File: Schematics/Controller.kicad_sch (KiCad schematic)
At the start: 0 parts

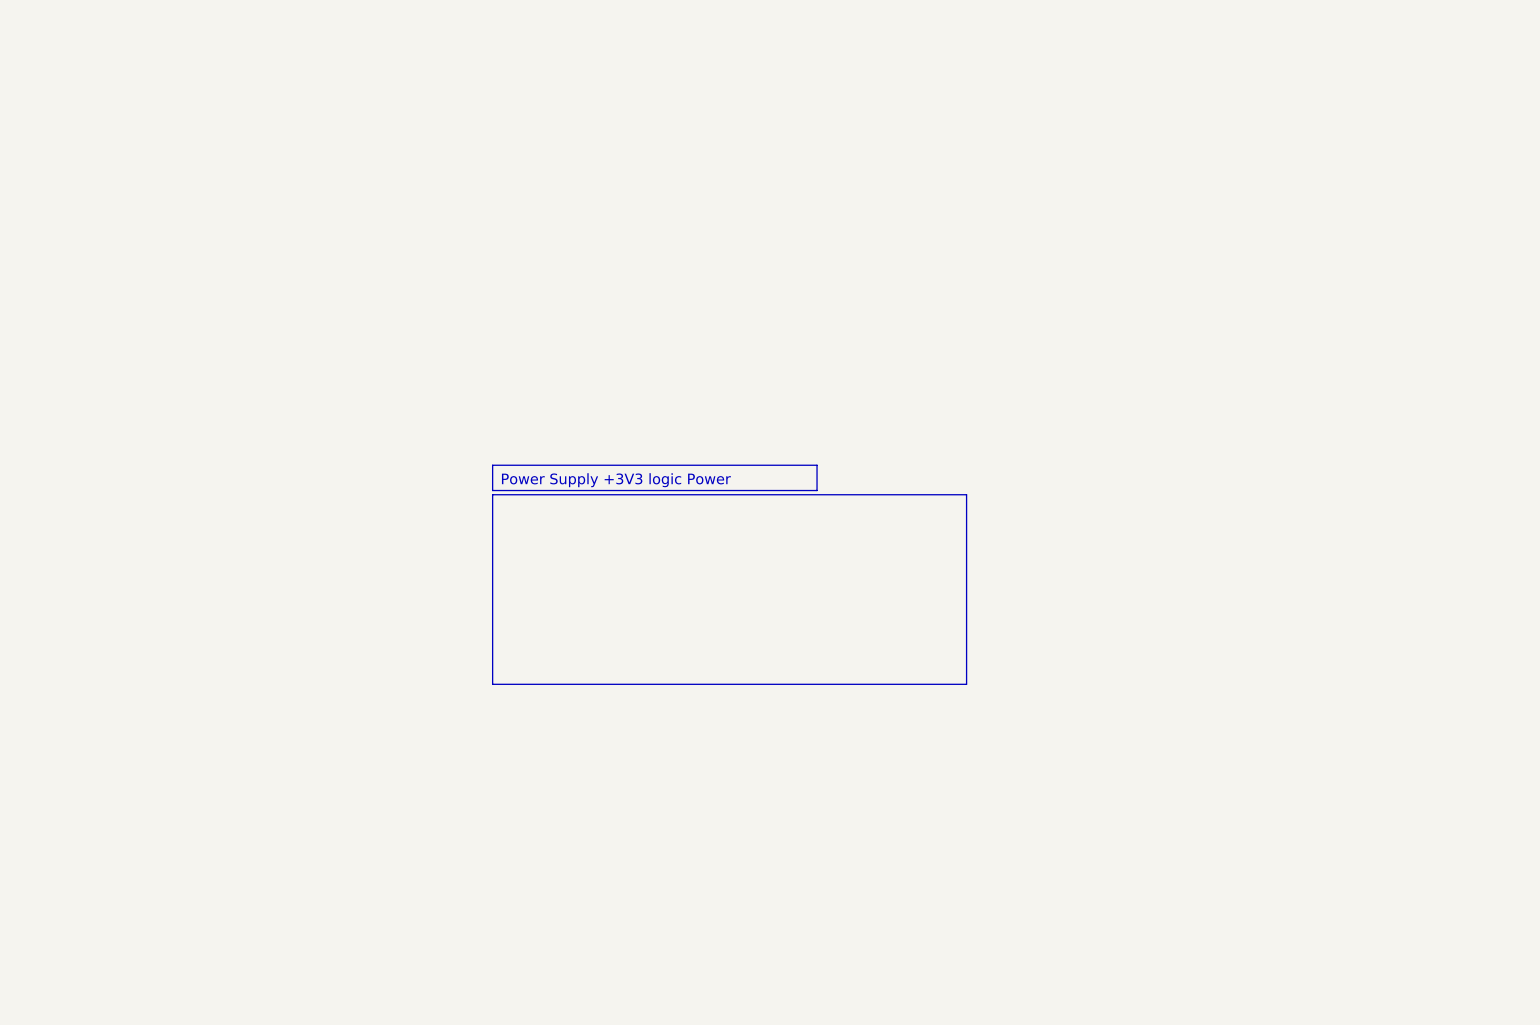
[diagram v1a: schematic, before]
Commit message: [WIP SiC Single Phase Inverter]
- Updated README to have a Block Diagram
- WIP Sub sheets Power, Controller
- Added the F2800 controller to the project
- Added the controller to the controller sub sheet
- Added text for a 15V to 3V3 voltage converter
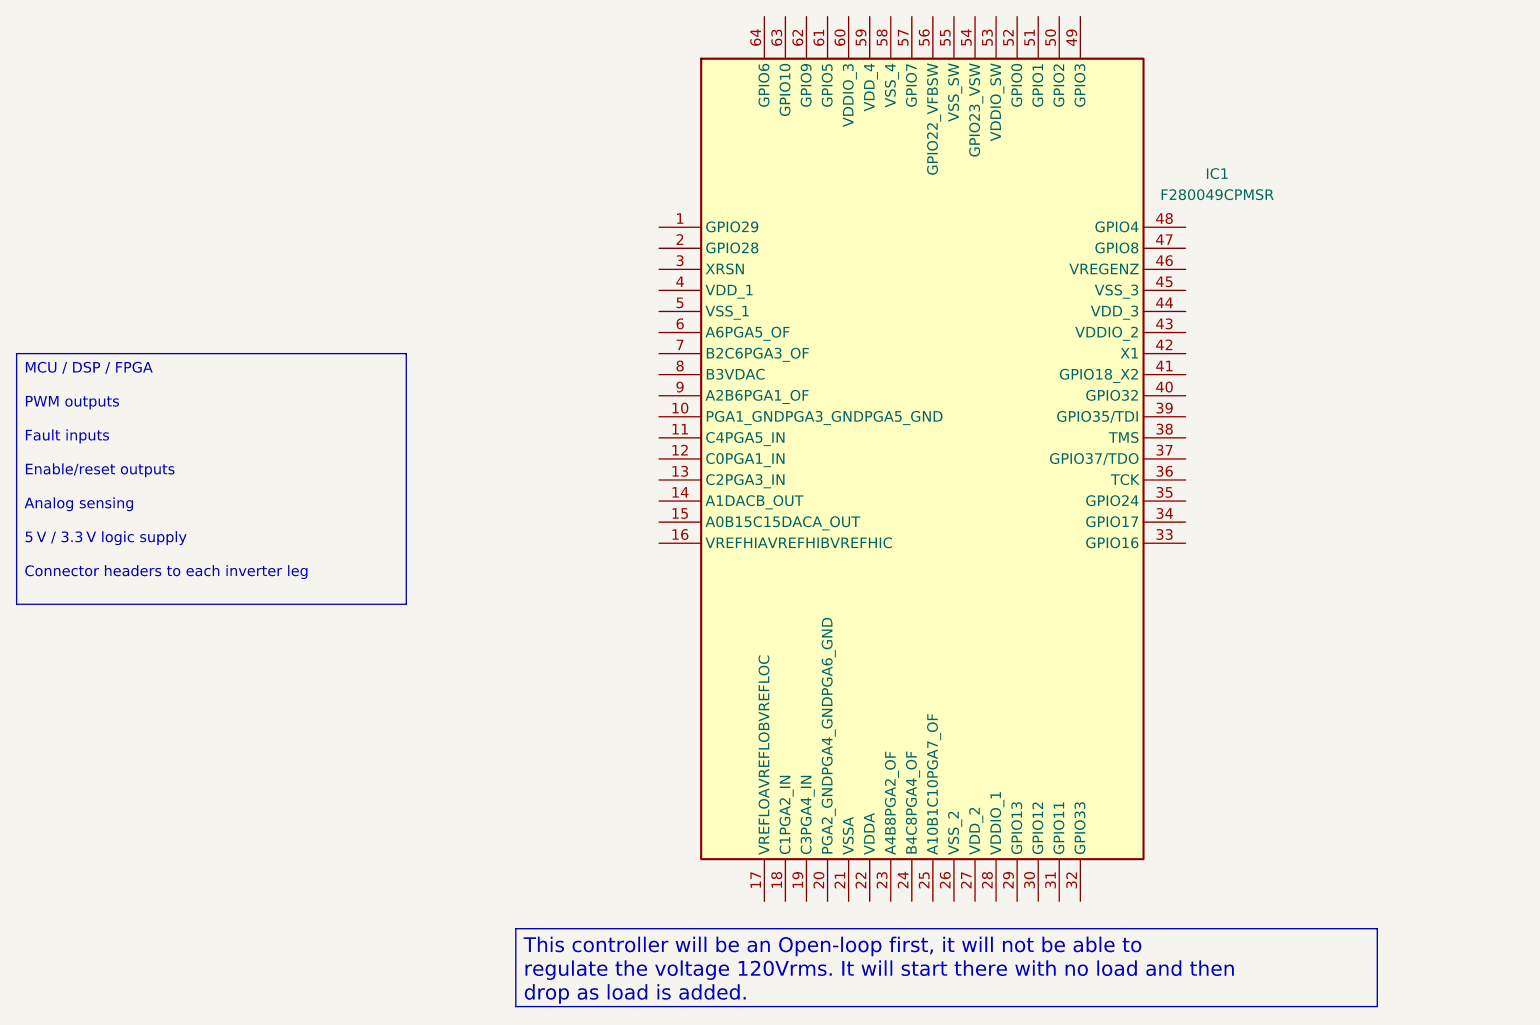
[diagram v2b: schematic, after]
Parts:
- added IC1: F280049CPMSR, SiC_Inverter:F280049CPMSR, symbol SiC_Inverter:F280049CPMSR

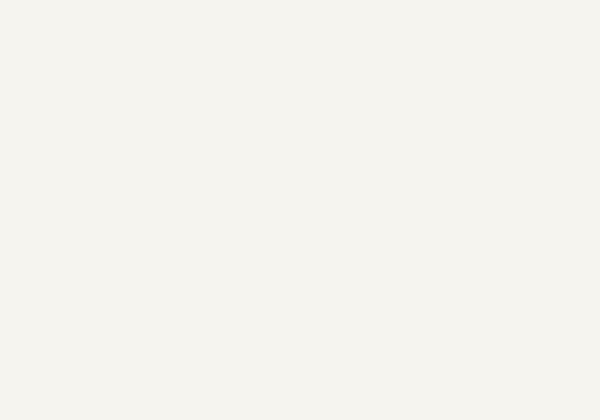
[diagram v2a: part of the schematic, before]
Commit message: [WIP Single Phase Inverter]
- Changed all Refs within each sub sheet (Stripe)
- Added 3V3 Power Supply off of 15V iso supply
- Added footprint, symbol and 3d part
- updated PCB with new part
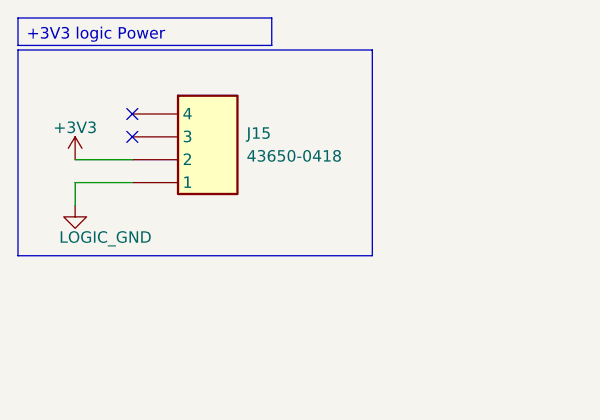
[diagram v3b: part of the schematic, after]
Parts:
- added J15: 43650-0418, SiC_Inverter:436500418, symbol SiC_Inverter:43650-0418
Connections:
- new net +3V3: J15.2
- new net LOGIC_GND: J15.1
- no-connect marks 0 -> 2

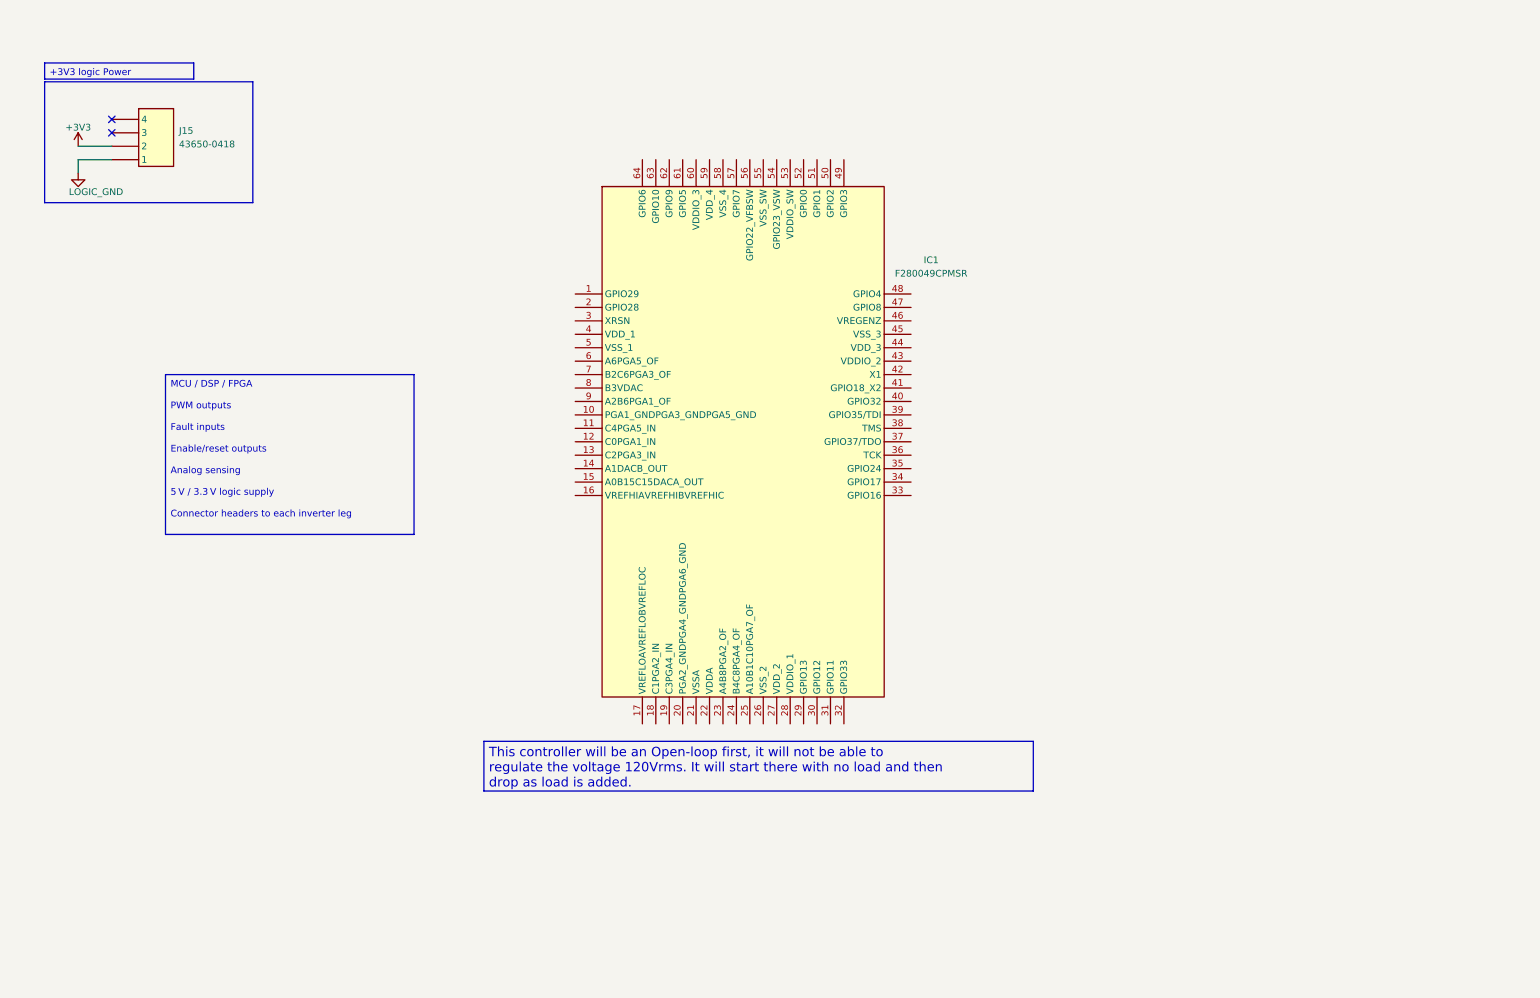
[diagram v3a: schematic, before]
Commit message: WIP: Work on Controller layout, and fixed some sheet text and positions
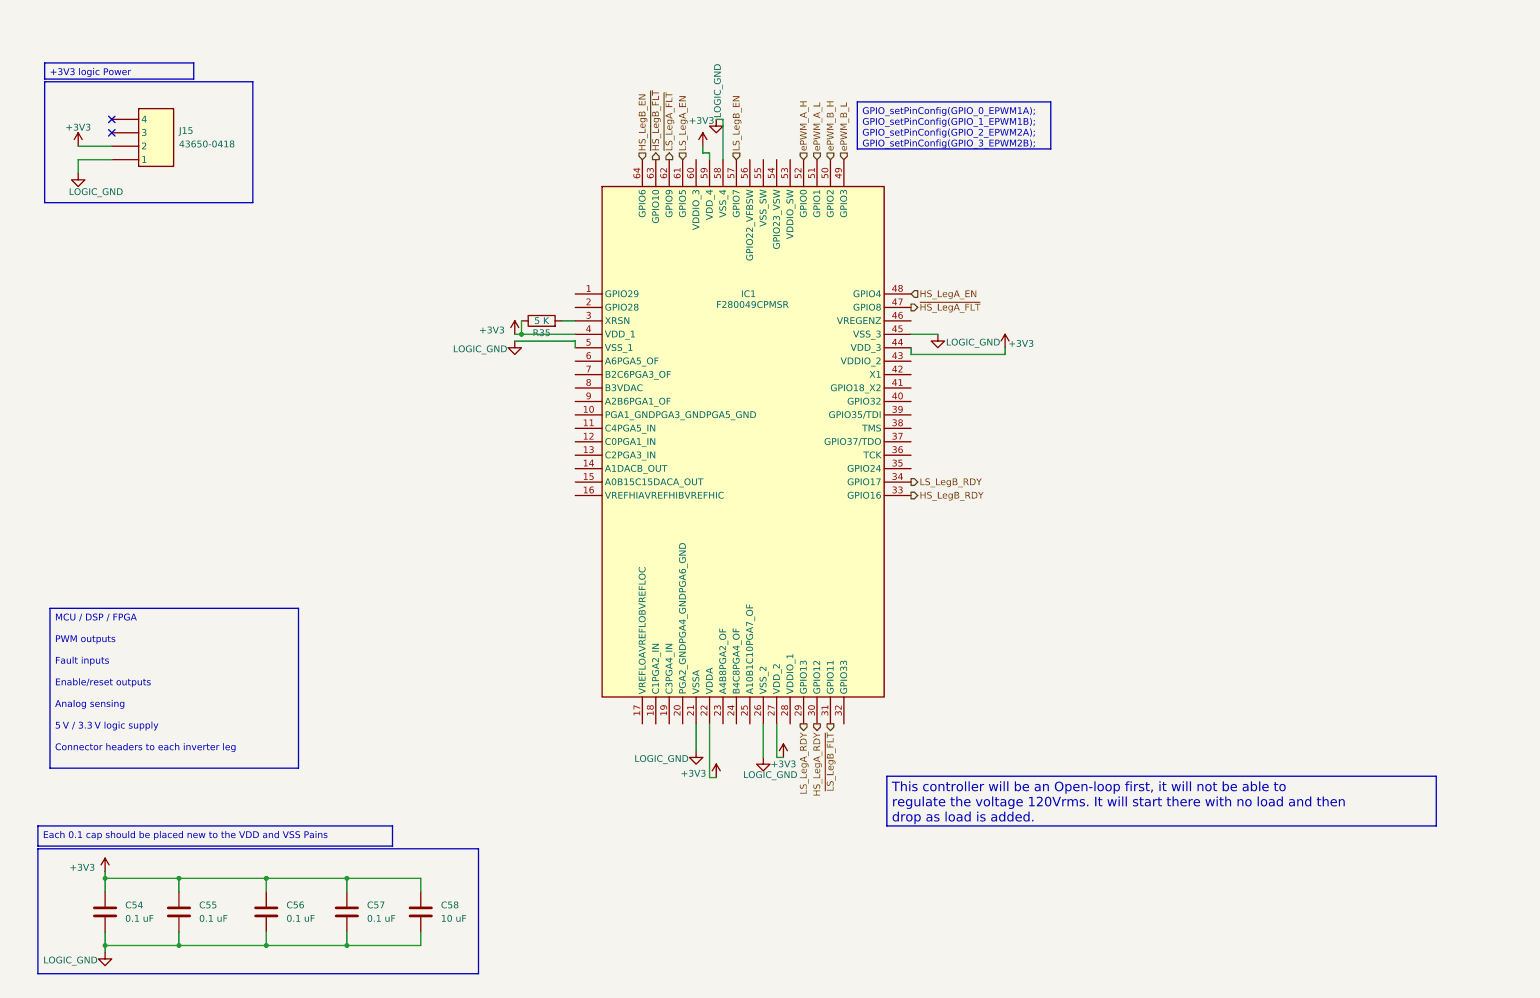
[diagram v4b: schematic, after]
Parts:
- added C54, C55, C56, C57: 0.1 uF, Capacitor_SMD:C_0805_2012Metric_Pad1.18x1.45mm_HandSolder, symbol SiC_Inverter:C2012X8R1E105M125AE
- added C58: 10 uF, Capacitor_SMD:C_0805_2012Metric_Pad1.18x1.45mm_HandSolder, symbol SiC_Inverter:C2012X5R1A106K085AC
- added R35: 5 K, Resistor_SMD:R_1206_3216Metric_Pad1.30x1.75mm_HandSolder, symbol SiC_Inverter:RT1206BRD075KL
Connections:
- net +3V3: now also IC1.22 (VDDA), IC1.27 (VDD_2), IC1.4 (VDD_1), IC1.44 (VDD_3), IC1.59 (VDD_4), C54.1, C55.1, C56.1, C57.1, C58.1, R35.1
- net LOGIC_GND: now also IC1.21 (VSSA), IC1.26 (VSS_2), IC1.45 (VSS_3), IC1.5 (VSS_1), IC1.58 (VSS_4), C54.2, C55.2, C56.2, C57.2, C58.2
- net LS_LegA_RDY: now reaches IC1.29 (GPIO13)
- net at IC1.3 (XRSN): now also R35.2
- net HS_LegA_RDY: now reaches IC1.30 (GPIO12)
- net ~{LS_LegB_FLT}: now reaches IC1.31 (GPIO11)
- net HS_LegB_RDY: now reaches IC1.33 (GPIO16)
- net LS_LegB_RDY: now reaches IC1.34 (GPIO17)
- net ~{HS_LegA_FLT}: now reaches IC1.47 (GPIO8)
- net HS_LegA_EN: now reaches IC1.48 (GPIO4)
- net ePWM_B_L: now reaches IC1.49 (GPIO3)
- net ePWM_B_H: now reaches IC1.50 (GPIO2)
- net ePWM_A_L: now reaches IC1.51 (GPIO1)
- net ePWM_A_H: now reaches IC1.52 (GPIO0)
- net LS_LegB_EN: now reaches IC1.57 (GPIO7)
- net LS_LegA_EN: now reaches IC1.61 (GPIO5)
- net ~{LS_LegA_FLT}: now reaches IC1.62 (GPIO9)
- net ~{HS_LegB_FLT}: now reaches IC1.63 (GPIO10)
- net HS_LegB_EN: now reaches IC1.64 (GPIO6)

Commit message: [WIP Controller Design]
- Wired up all 64 Pins on the Controller
- Added 3d models for connectors and Controller
- Added data sheets for the newly added parts
- wired connectors to controller to external PCB Boards
- Updated Text fields
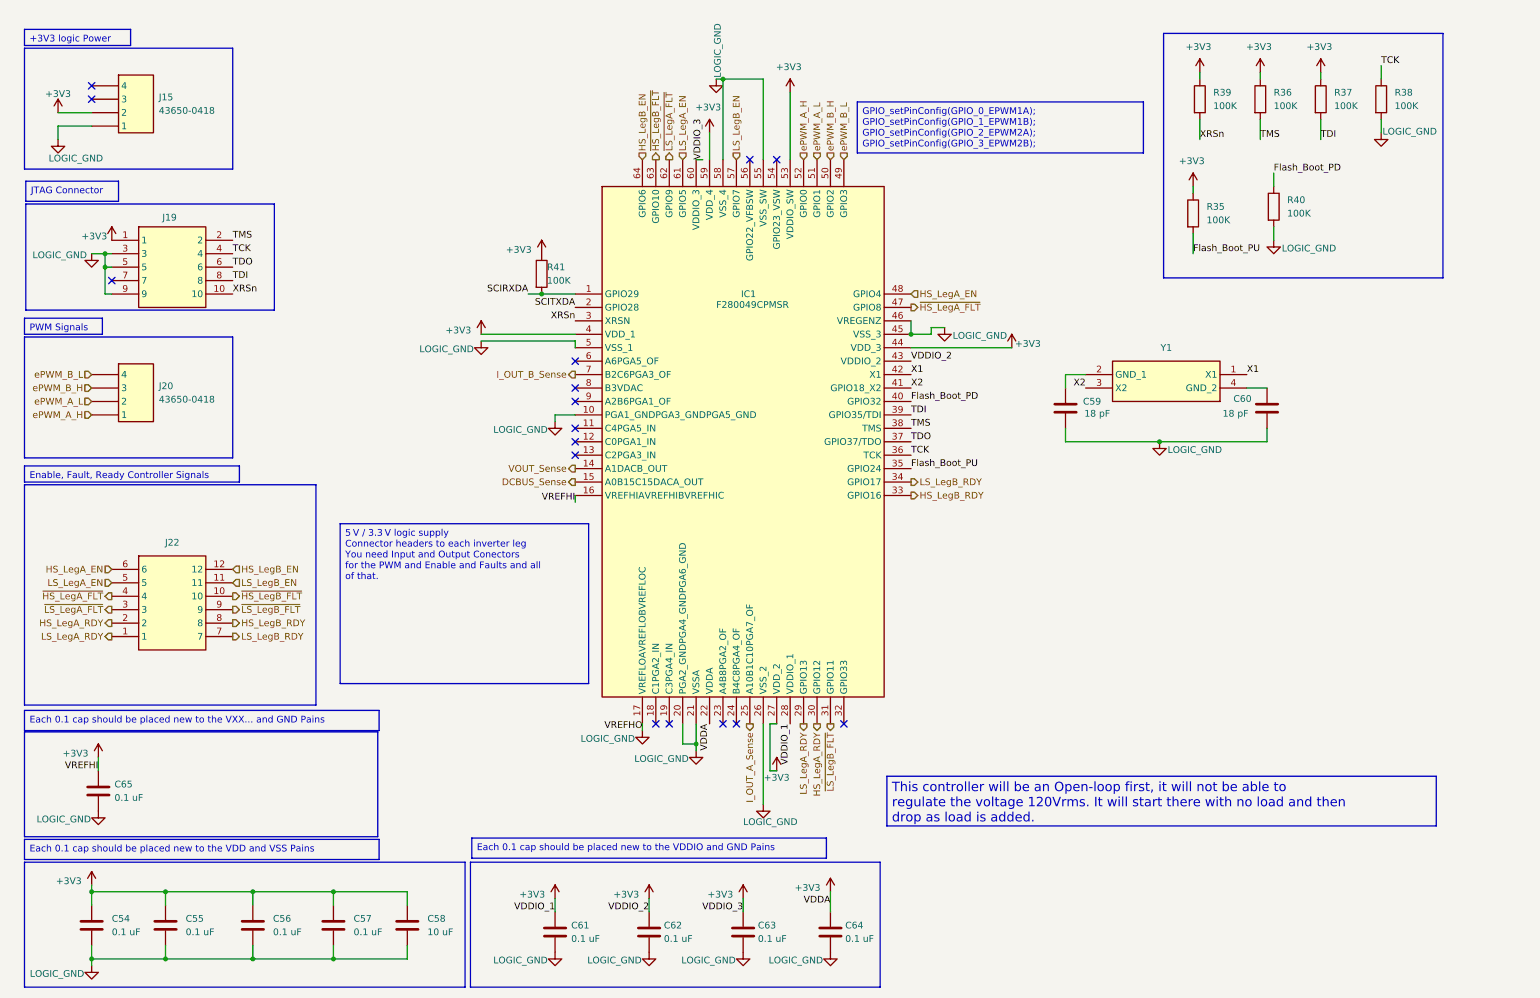
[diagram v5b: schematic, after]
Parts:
- removed R35: 5 K, Resistor_SMD:R_1206_3216Metric_Pad1.30x1.75mm_HandSolder, symbol SiC_Inverter:RT1206BRD075KL
- added C59, C60: 18 pF, Capacitor_SMD:C_0402_1005Metric_Pad0.74x0.62mm_HandSolder, symbol SiC_Inverter:C2012X8R1E105M125AE
- added C61, C62, C63, C64, C65: 0.1 uF, Capacitor_SMD:C_0805_2012Metric_Pad1.18x1.45mm_HandSolder, symbol SiC_Inverter:C2012X8R1E105M125AE
- added J19: FTSH-105-01-LM-D-K, SiC_Inverter:FTSH-105-01-LM-D-K, symbol SiC_Inverter:FTSH-105-01-LM-D-K
- added J20: 43650-0418, SiC_Inverter:436500418, symbol SiC_Inverter:43650-0418
- added J22: 43045-1212, SiC_Inverter:43045-1212, symbol SiC_Inverter:43045-1212
- added R35, R36, R37, R38, R39, R40, R41: 100K, Resistor_SMD:R_1206_3216Metric_Pad1.30x1.75mm_HandSolder, symbol Device:R
- added Y1: ABM8-20.000MHZ-B2-T, SiC_Inverter:ABM8-20.000MHZ-B2-T, symbol SiC_Inverter:ABM8-20.000MHZ-B2-T
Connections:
- net +3V3: now also IC1.16 (VREFHIAVREFHIBVREFHIC), IC1.28 (VDDIO_1), IC1.43 (VDDIO_2), IC1.53 (VDDIO_SW), IC1.60 (VDDIO_3), C61.1, C62.1, C63.1, C64.1, C65.1, J19.1, R35.1, R36.1, R37.1, R39.1, R41.1
- net HS_LegA_EN: now also J22.6
- net HS_LegA_RDY: now also J22.2
- net HS_LegB_EN: now also J22.12
- net HS_LegB_RDY: now also J22.8
- net LOGIC_GND: now also IC1.10 (PGA1_GNDPGA3_GNDPGA5_GND), IC1.17 (VREFLOAVREFLOBVREFLOC), IC1.20 (PGA2_GNDPGA4_GNDPGA6_GND), IC1.46 (VREGENZ), IC1.55 (VSS_SW), C59.2, C60.2, C61.2, C62.2, C63.2, C64.2, C65.2, J19.3, J19.5, J19.9, R38.2, R40.2
- net LS_LegA_EN: now also J22.5
- net LS_LegA_RDY: now also J22.1
- net LS_LegB_EN: now also J22.11
- net LS_LegB_RDY: now also J22.7
- net ePWM_A_H: now also J20.1
- net ePWM_A_L: now also J20.2
- net ePWM_B_H: now also J20.3
- net ePWM_B_L: now also J20.4
- net ~{HS_LegA_FLT}: now also J22.4
- net ~{HS_LegB_FLT}: now also J22.10
- net ~{LS_LegA_FLT}: now also J22.3
- net ~{LS_LegB_FLT}: now also J22.9
- net XRSn: now reaches IC1.3 (XRSN)
- net XRSn: now also J19.10, R39.2
- net SCIRXDA: now reaches IC1.1 (GPIO29)
- net SCIRXDA: now also R41.2
- net VOUT_Sense: now reaches IC1.14 (A1DACB_OUT)
- net DCBUS_Sense: now reaches IC1.15 (A0B15C15DACA_OUT)
- net SCITXDA: now reaches IC1.2 (GPIO28)
- net I_OUT_A_Sense: now reaches IC1.25 (A10B1C10PGA7_OF)
- net Flash_Boot_PU: now reaches IC1.35 (GPIO24)
- net Flash_Boot_PU: now also R35.2
- net TCK: now reaches IC1.36 (TCK)
- net TCK: now also J19.4, R38.1
- net TDO: now reaches IC1.37 (GPIO37/TDO)
- net TDO: now also J19.6
- net TMS: now reaches IC1.38 (TMS)
- net TMS: now also J19.2, R36.2
- net TDI: now reaches IC1.39 (GPIO35/TDI)
- net TDI: now also J19.8, R37.2
- net Flash_Boot_PD: now reaches IC1.40 (GPIO32)
- net Flash_Boot_PD: now also R40.1
- net X2: now reaches IC1.41 (GPIO18_X2)
- net X2: now also Y1.3 (X2)
- net X1: now reaches IC1.42 (X1)
- net X1: now also Y1.1 (X1)
- net I_OUT_B_Sense: now reaches IC1.7 (B2C6PGA3_OF)
- new net: C60.1, Y1.4 (GND_2)
- new net: C59.1, Y1.2 (GND_1)
- no-connect marks 2 -> 16
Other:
- moved on the sheet: C54, C55, C56, C57, C58, J15
